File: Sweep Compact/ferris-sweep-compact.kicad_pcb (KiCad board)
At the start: 2 copper layers, 107.2 x 86.9 mm, 21 parts, among them J1 MJ-4PP-9, SW10 SW_PUSH, SW11 SW_PUSH, SW12 SW_PUSH, SW14 SW_PUSH, SW15 SW_PUSH, SW16 SW_PUSH, SW17 SW_PUSH, SW18 SW_PUSH, SW2 SW_PUSH, SW20 SW_PUSH, SW21 SW_PUSH, SW3 SW_PUSH, SW4 SW_PUSH, SW5 SW_PUSH, SW6 SW_PUSH, SW8 SW_PUSH, SW9 SW_PUSH, U1 ProMicro

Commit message: update stagger
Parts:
- moved SW10 1.95 mm to (80.0, 40.7)
- moved SW16 1.95 mm to (80.0, 57.7)
- moved SW4 1.95 mm to (80.0, 23.7)
- moved SW17 1.20 mm to (98.0, 63.3)
- moved SW5 1.20 mm to (98.0, 29.3)
- moved SW11 1.20 mm to (98.0, 46.3)
- moved SW12 0.70 mm to (116.0, 48.7)
- moved SW18 0.70 mm to (116.0, 65.7)
- moved SW6 0.70 mm to (116.0, 31.7)
- moved RSW1 0.40 mm to (127.0, 77.6)
- moved SW14 0.40 mm to (44.0, 76.8)
- moved SW15 0.40 mm to (62.0, 64.5)
- moved SW2 0.40 mm to (44.0, 42.8)
- moved SW8 0.40 mm to (44.0, 59.8)
- moved SW3 0.40 mm to (62.0, 30.5)
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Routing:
- net GND: track 473.9 -> 490.3 mm
- net Net-(U1-Pad14): track 58.0 -> 62.1 mm
- net SCL: track 100.6 -> 103.5 mm
- net col5: track 79.9 -> 82.7 mm
- net SDA: track 131.2 -> 133.9 mm
- net Net-(U1-Pad13): track 37.6 -> 40.3 mm
- net col4: track 105.7 -> 107.3 mm
- net row1: track 56.0 -> 57.5 mm
- net col3: track 88.8 -> 87.5 mm
- net row0: track 77.7 -> 78.8 mm
- net row3: track 142.4 -> 143.0 mm
- net col0: track 22.1 -> 22.6 mm

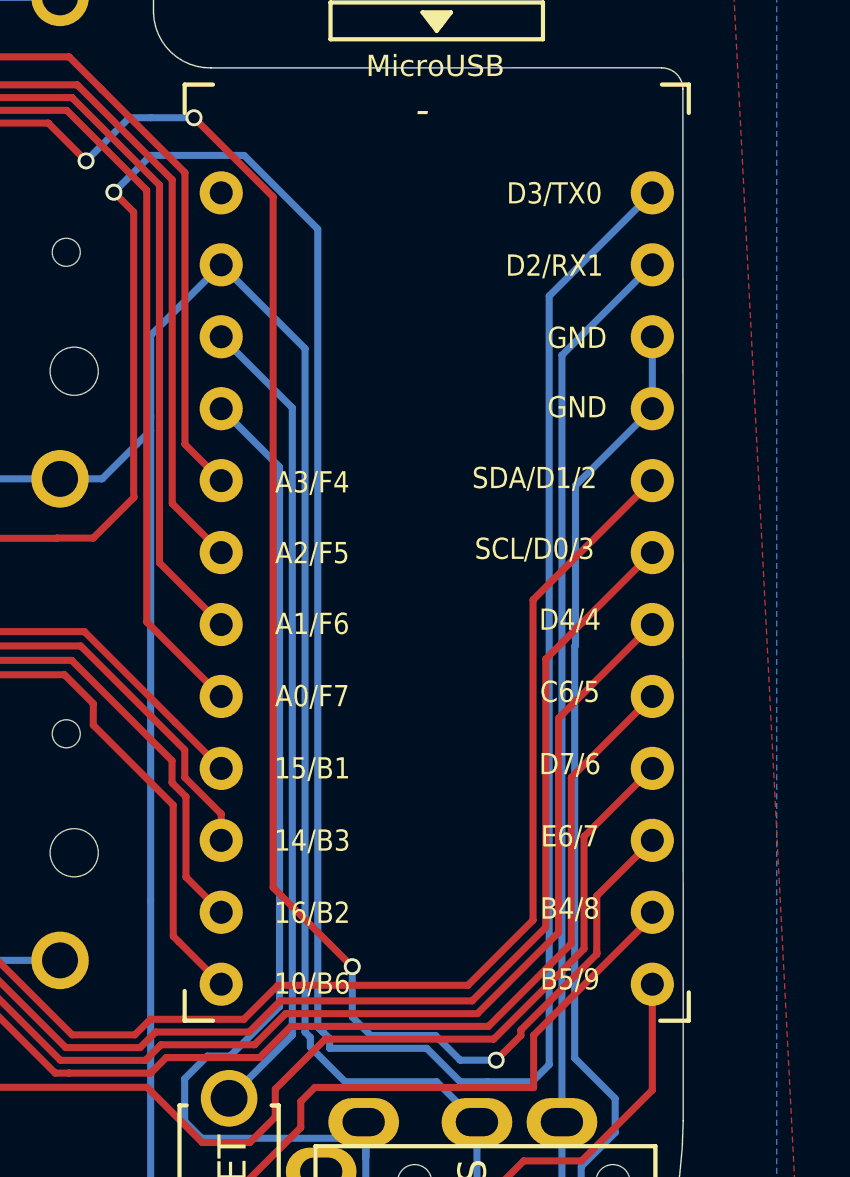
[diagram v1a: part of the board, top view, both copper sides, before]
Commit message: Add controller directional hint to pcb as well.
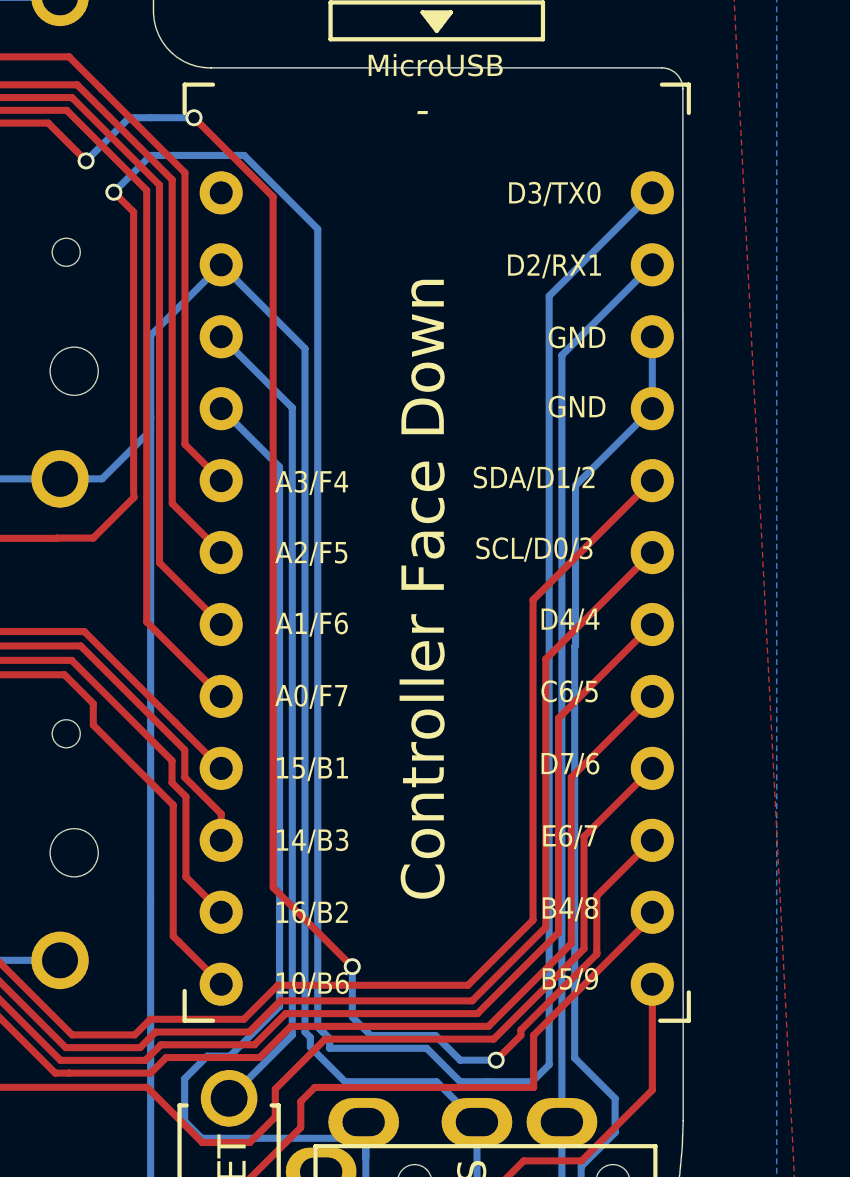
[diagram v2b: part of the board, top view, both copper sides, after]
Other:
- board text added: "Controller Face Down"
- board text added: "Controller Face Up"
